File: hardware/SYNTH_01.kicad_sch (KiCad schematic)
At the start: 58 parts, among them J2 Conn_01x04_Pin, SW1 SW_Push_45deg, SW10 SW_Push_45deg, SW11 SW_Push_45deg, SW12 SW_Push_45deg, SW13 SW_Push_45deg, SW14 SW_Push_45deg, SW15 SW_Push_45deg, SW16 SW_Push_45deg, SW17 SW_Push_45deg, SW18 SW_Push_45deg, SW19 SW_Push_45deg, SW2 SW_Push_45deg, SW20 SW_Push_45deg, SW21 SW_Push_45deg, SW3 SW_Push_45deg, SW4 SW_Push_45deg, SW5 SW_Push_45deg, SW6 SW_Push_45deg, SW7 SW_Push_45deg, SW8 SW_Push_45deg, SW9 SW_Push_45deg, U1 MCP23017-E/SP, U2 MCP23017-E/SP

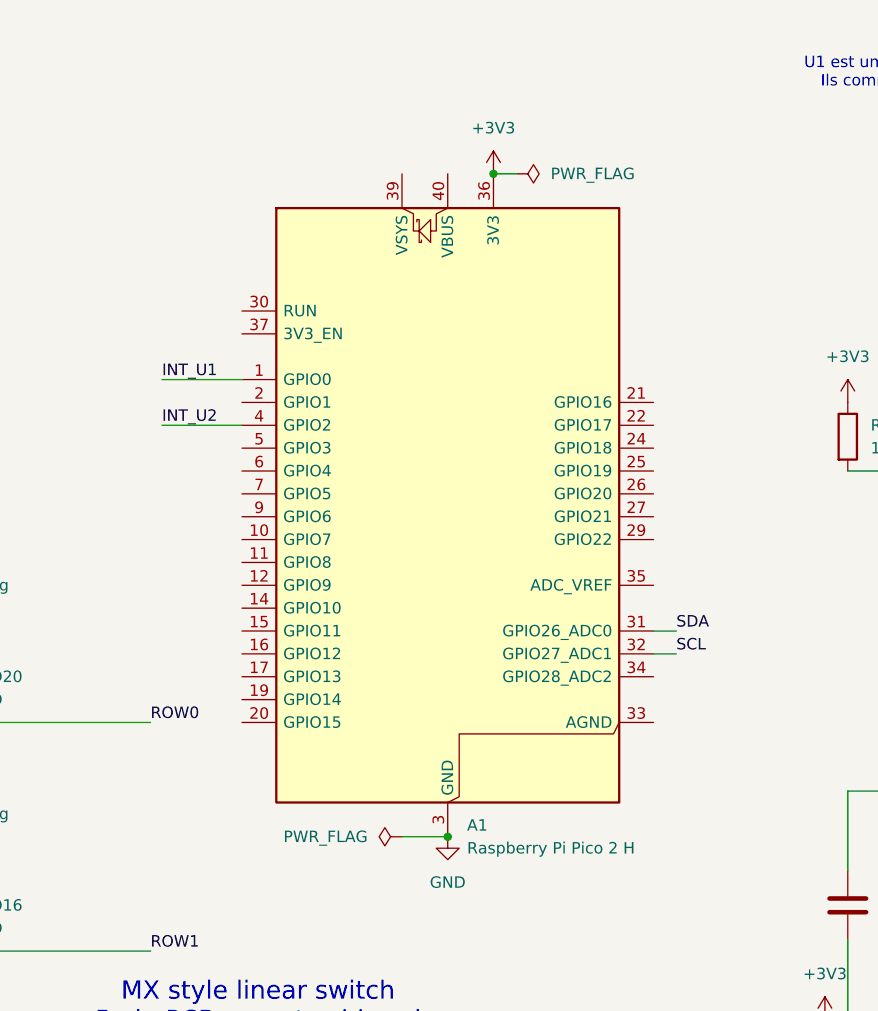
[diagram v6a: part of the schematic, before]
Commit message: [PCB] moving SDA to A1.1 & SCL to A1.2 & fixing power flags
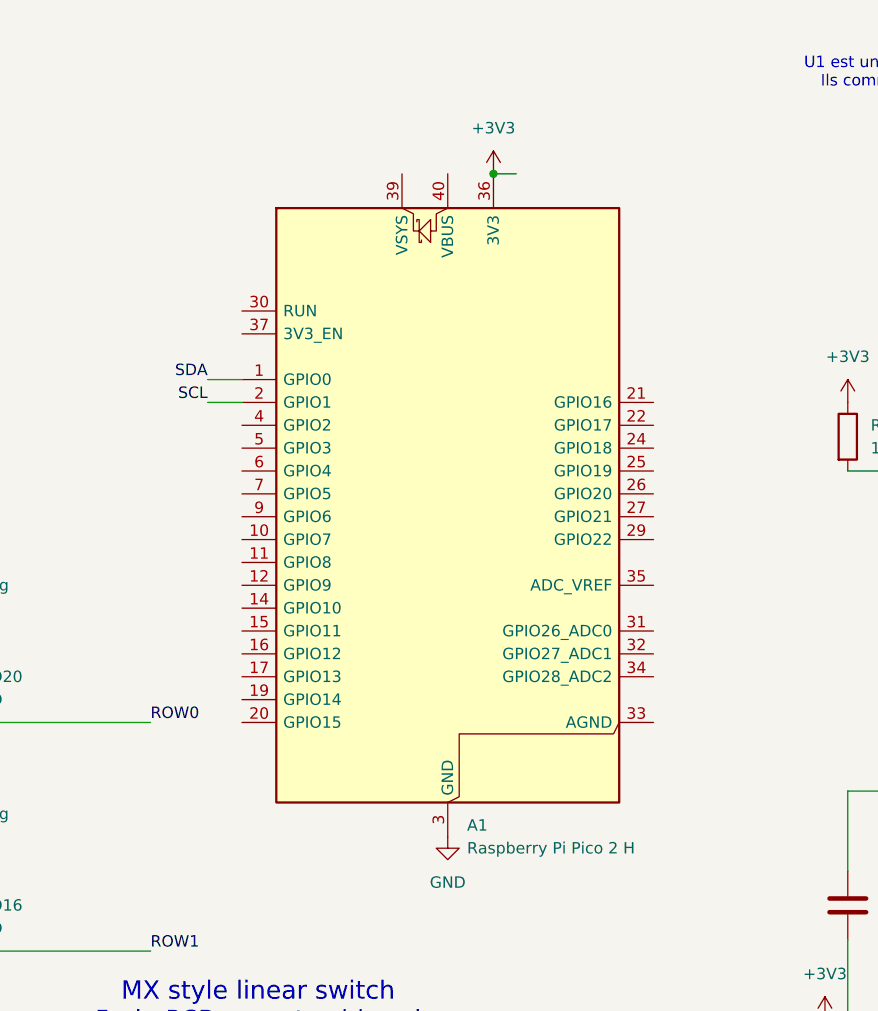
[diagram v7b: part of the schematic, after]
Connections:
- net INT_U1: no longer A1.1 (GPIO0)
- net INT_U2: no longer A1.4 (GPIO2)
- net SCL: now also A1.2 (GPIO1); no longer A1.32 (GPIO27_ADC1)
- net SDA: now also A1.1 (GPIO0); no longer A1.31 (GPIO26_ADC0)
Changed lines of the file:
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@@
 	)
 	(junction
-		(at 189.23 106.68)
-		(diameter 0)
-		(color 0 0 0 0)
-	)
-	(junction
 		(at 130.81 106.68)
 		(diameter 0)
@@
 	(wire
 		(pts
-			(xy 157.48 60.96) (xy 166.37 60.96)
-		)
-		(stroke
-			(width 0)
-			(type default)
-		)
-	)
-	(wire
-		(pts
 			(xy 237.49 40.64) (xy 242.57 40.64)
 		)
@@
 	(wire
 		(pts
+			(xy 162.56 55.88) (xy 166.37 55.88)
+		)
+		(stroke
+			(width 0)
+			(type default)
+		)
+	)
+	(wire
+		(pts
 			(xy 80.01 106.68) (xy 80.01 132.08)
 		)
@@
 	(wire
 		(pts
-			(xy 22.86 149.86) (xy 30.48 149.86)
+			(xy 162.56 58.42) (xy 166.37 58.42)
 		)
 		(stroke
@@
 	(wire
 		(pts
-			(xy 43.18 195.58) (xy 59.69 195.58)
+			(xy 22.86 149.86) (xy 30.48 149.86)
 		)
 		(stroke
@@
 	(wire
 		(pts
-			(xy 85.09 119.38) (xy 110.49 119.38)
+			(xy 43.18 195.58) (xy 59.69 195.58)
 		)
 		(stroke
@@
 	(wire
 		(pts
-			(xy 212.09 86.36) (xy 214.63 86.36)
+			(xy 85.09 119.38) (xy 110.49 119.38)
 		)
 		(stroke
@@
 	(wire
 		(pts
-			(xy 157.48 55.88) (xy 166.37 55.88)
-		)
-		(stroke
-			(width 0)
-			(type default)
-		)
-	)
-	(wire
-		(pts
 			(xy 267.97 121.92) (xy 271.78 121.92)
 		)
@@
 	(wire
 		(pts
-			(xy 184.15 106.68) (xy 189.23 106.68)
-		)
-		(stroke
-			(width 0)
-			(type default)
-		)
-	)
-	(wire
-		(pts
 			(xy 24.13 95.25) (xy 30.48 95.25)
 		)
@@
 	(wire
 		(pts
-			(xy 212.09 83.82) (xy 214.63 83.82)
-		)
-		(stroke
-			(width 0)
-			(type default)
-		)
-	)
-	(wire
-		(pts
 			(xy 135.89 170.18) (xy 156.21 170.18)
 		)
@@
 		)
 	)
-	(label "SCL"
-		(at 214.63 86.36 0)
-		(effects
-			(font
-				(size 1.27 1.27)
-			)
-			(justify left bottom)
-		)
-	)
 	(label "GND"
 		(at 234.95 147.32 0)
@@
 		)
 	)
-	(label "SDA"
-		(at 214.63 83.82 0)
-		(effects
-			(font
-				(size 1.27 1.27)
-			)
-			(justify left bottom)
-		)
-	)
 	(label "E4_B"
 		(at 271.78 124.46 0)
@@
 		)
 	)
-	(label "ROW1"
-		(at 156.21 119.38 0)
+	(label "SCL"
+		(at 162.56 58.42 180)
 		(effects
 			(font
 				(size 1.27 1.27)
 			)
-			(justify left bottom)
+			(justify right bottom)
 		)
 	)
-	(label "COL3"
-		(at 271.78 68.58 0)
+	(label "ROW1"
+		(at 156.21 119.38 0)
 		(effects
 			(font
@@
 		)
 	)
-	(label "INT_U1"
-		(at 157.48 55.88 0)
+	(label "COL3"
+		(at 271.78 68.58 0)
 		(effects
 			(font
@@
 		)
 	)
-	(label "INT_U2"
-		(at 157.48 60.96 0)
+	(label "COL0"
+		(at 271.78 60.96 0)
 		(effects
 			(font
@@
 		)
 	)
-	(label "COL0"
-		(at 271.78 60.96 0)
+	(label "E1_A"
+		(at 271.78 106.68 0)
 		(effects
 			(font
@@
 		)
 	)
-	(label "E1_A"
-		(at 271.78 106.68 0)
+	(label "SDA"
+		(at 162.56 55.88 180)
 		(effects
 			(font
 				(size 1.27 1.27)
 			)
-			(justify left bottom)
+			(justify right bottom)
 		)
 	)
@@
 	)
 	(symbol
-		(lib_id "power:PWR_FLAG")
-		(at 184.15 106.68 90)
-		(unit 1)
-		(body_style 1)
-		(exclude_from_sim no)
-		(in_bom yes)
-		(on_board yes)
-		(in_pos_files yes)
-		(dnp no)
-		(fields_autoplaced yes)
-		(property "Reference" "#FLG02"
-			(at 182.245 106.68 0)
-			(hide yes)
-			(show_name no)
-			(do_not_autoplace no)
-			(effects
-				(font
-					(size 1.27 1.27)
-				)
-			)
-		)
-		(property "Value" "PWR_FLAG"
-			(at 180.34 106.6799 90)
-			(show_name no)
-			(do_not_autoplace no)
-			(effects
-				(font
-					(size 1.27 1.27)
-				)
-				(justify left)
-			)
-		)
-		(property "Footprint" ""
-			(at 184.15 106.68 0)
-			(hide yes)
-			(show_name no)
-			(do_not_autoplace no)
-			(effects
-				(font
-					(size 1.27 1.27)
-				)
-			)
-		)
-		(property "Datasheet" ""
-			(at 184.15 106.68 0)
-			(hide yes)
-			(show_name no)
-			(do_not_autoplace no)
-			(effects
-				(font
-					(size 1.27 1.27)
-				)
-			)
-		)
-		(property "Description" "Special symbol for telling ERC where power comes from"
-			(at 184.15 106.68 0)
-			(hide yes)
-			(show_name no)
-			(do_not_autoplace no)
-			(effects
-				(font
-					(size 1.27 1.27)
-				)
-			)
-		)
-		(pin "1"
-		)
-		(instances
-			(project "SYNTH_01"
-				(path "/8736209f-7c7b-4c76-92ee-96040748110a"
-					(reference "#FLG02")
-					(unit 1)
-				)
-			)
-		)
-	)
-	(symbol
 		(lib_id "power:GND")
 		(at 255.27 85.09 0)
@@
 					(unit 1)
 				)
-			)
-		)
-	)
-	(symbol
-		(lib_id "power:PWR_FLAG")
-		(at 196.85 33.02 270)
-		(unit 1)
-		(body_style 1)
-		(exclude_from_sim no)
-		(in_bom yes)
-		(on_board yes)
-		(in_pos_files yes)
-		(dnp no)
-		(fields_autoplaced yes)
-		(property "Reference" "#FLG01"
-			(at 198.755 33.02 0)
-			(hide yes)
-			(show_name no)
-			(do_not_autoplace no)
-			(effects
-				(font
-					(size 1.27 1.27)
-				)
-			)
-		)
-		(property "Value" "PWR_FLAG"
-			(at 200.66 33.0199 90)
-			(show_name no)
-			(do_not_autoplace no)
-			(effects
-				(font
-					(size 1.27 1.27)
-				)
-				(justify left)
-			)
-		)
-		(property "Footprint" ""
-			(at 196.85 33.02 0)
-			(hide yes)
-			(show_name no)
-			(do_not_autoplace no)
-			(effects
-				(font
-					(size 1.27 1.27)
-				)
-			)
-		)
-		(property "Datasheet" ""
-			(at 196.85 33.02 0)
-			(hide yes)
-			(show_name no)
-			(do_not_autoplace no)
-			(effects
-				(font
-					(size 1.27 1.27)
-				)
-			)
-		)
-		(property "Description" "Special symbol for telling ERC where power comes from"
-			(at 196.85 33.02 0)
-			(hide yes)
-			(show_name no)
-			(do_not_autoplace no)
-			(effects
-				(font
-					(size 1.27 1.27)
-				)
-			)
-		)
-		(pin "1"
-		)
-		(instances
-			(project "SYNTH_01"
-				(path "/8736209f-7c7b-4c76-92ee-96040748110a"
-					(reference "#FLG01")
-					(unit 1)
-				)

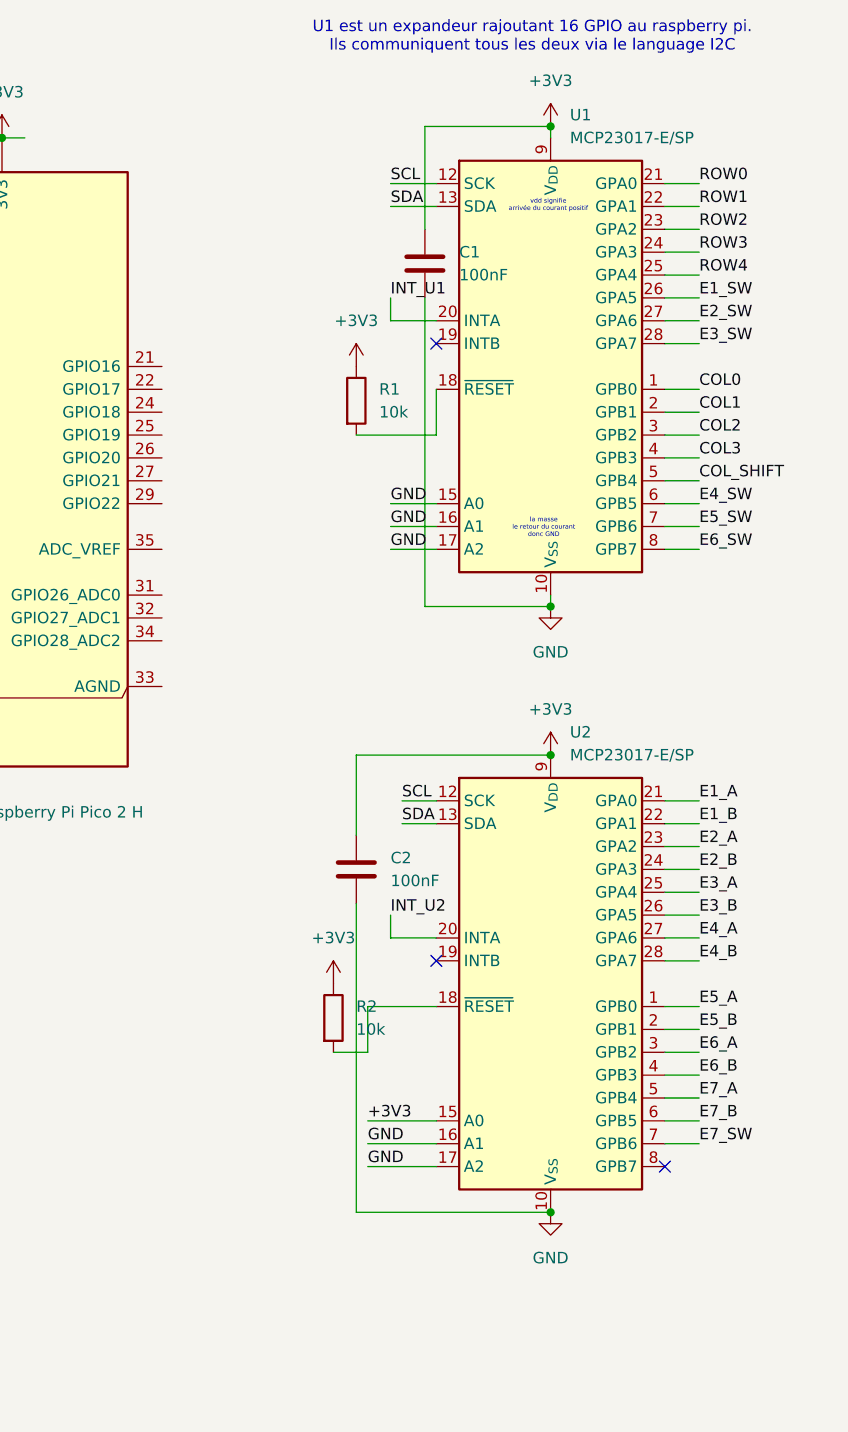
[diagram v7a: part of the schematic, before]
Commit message: [PCB] connecting matrix + encoders to U1
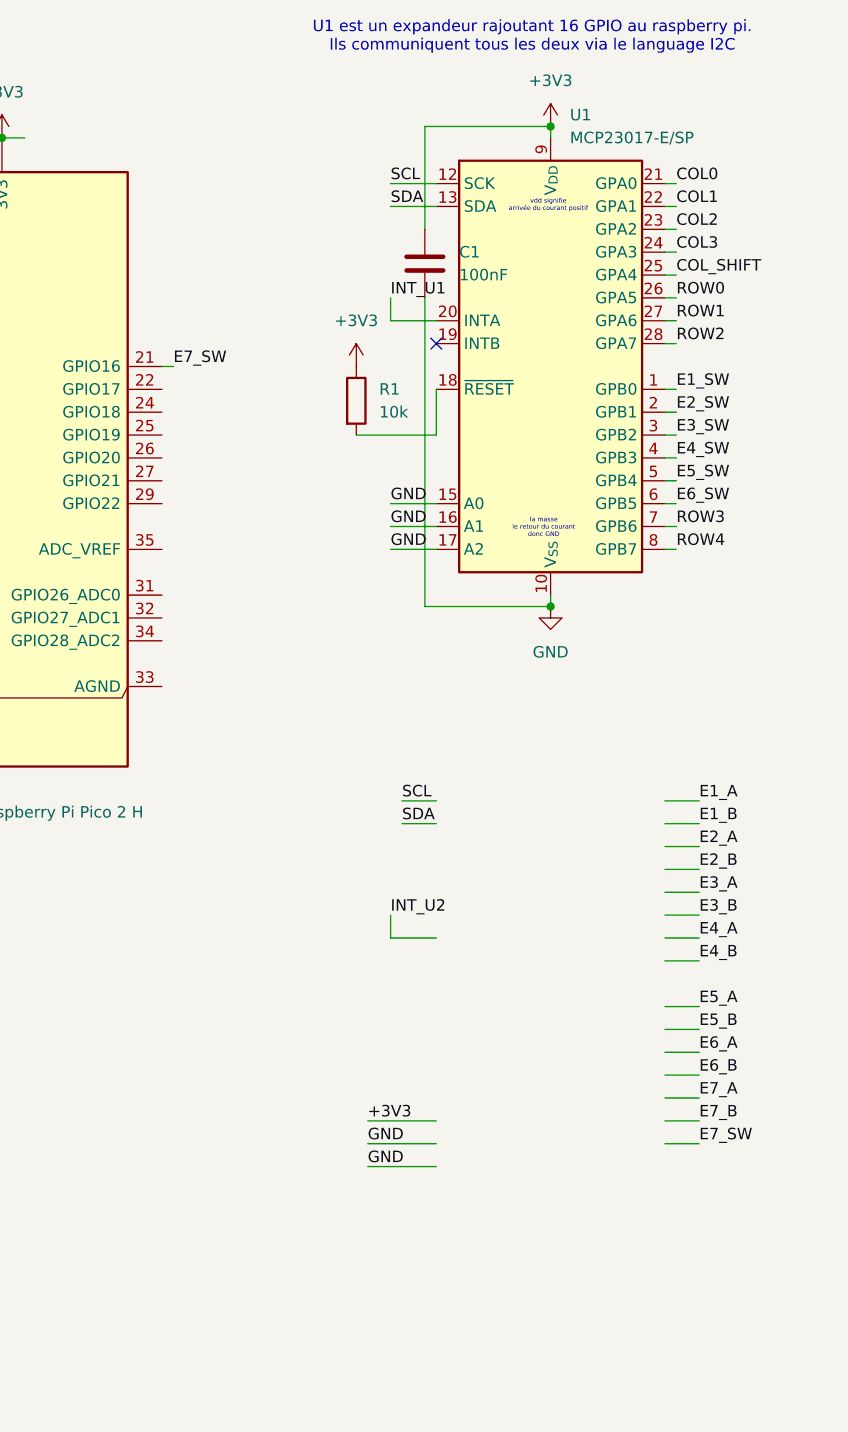
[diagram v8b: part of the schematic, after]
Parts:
- removed C2: 100nF, symbol Device:C
- removed R2: 10k, symbol Device:R
- removed U2: MCP23017-E/SP, Package_DIP:DIP-28_W7.62mm, symbol Interface_Expansion:MCP23017x-x-SP
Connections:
- net COL0: now also U1.21 (GPA0); no longer U1.1 (GPB0)
- net COL1: now also U1.22 (GPA1); no longer U1.2 (GPB1)
- net COL2: now also U1.23 (GPA2); no longer U1.3 (GPB2)
- net COL3: now also U1.24 (GPA3); no longer U1.4 (GPB3)
- net COL_SHIFT: now also U1.25 (GPA4); no longer U1.5 (GPB4)
- net E1_SW: now also U1.1 (GPB0); no longer U1.26 (GPA5)
- net E2_SW: now also U1.2 (GPB1); no longer U1.27 (GPA6)
- net E3_SW: now also U1.3 (GPB2); no longer U1.28 (GPA7)
- net E4_SW: now also U1.4 (GPB3); no longer U1.6 (GPB5)
- net E5_SW: now also U1.5 (GPB4); no longer U1.7 (GPB6)
- net E6_SW: now also U1.6 (GPB5); no longer U1.8 (GPB7)
- net E7_SW: now also A1.21 (GPIO16)
- net ROW0: now also U1.26 (GPA5); no longer U1.21 (GPA0)
- net ROW1: now also U1.27 (GPA6); no longer U1.22 (GPA1)
- net ROW2: now also U1.28 (GPA7); no longer U1.23 (GPA2)
- net ROW3: now also U1.7 (GPB6); no longer U1.24 (GPA3)
- net ROW4: now also U1.8 (GPB7); no longer U1.25 (GPA4)
- no-connect marks 3 -> 1
